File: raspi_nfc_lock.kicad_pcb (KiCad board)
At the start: 2 copper layers, 79 parts, among them J101 Raspberry_Pi_2_3, J102 Screw_Terminal_01x02, J103 Screw_Terminal_01x02, J104 Screw_Terminal_01x02, J105 Screw_Terminal_01x02, J106 Screw_Terminal_01x02, J107 Screw_Terminal_01x02, J108 Screw_Terminal_01x02, J109 Screw_Terminal_01x02, J110 Screw_Terminal_01x02, J111 Screw_Terminal_01x02, J112 Screw_Terminal_01x02, J113 BUZZER, K101 G6E, Q101 MMBT3904, Q102 Si2319CDS, Q103 MMBT3904, U101 74HC14, U102 LM2596S, U103 TXB0104PW

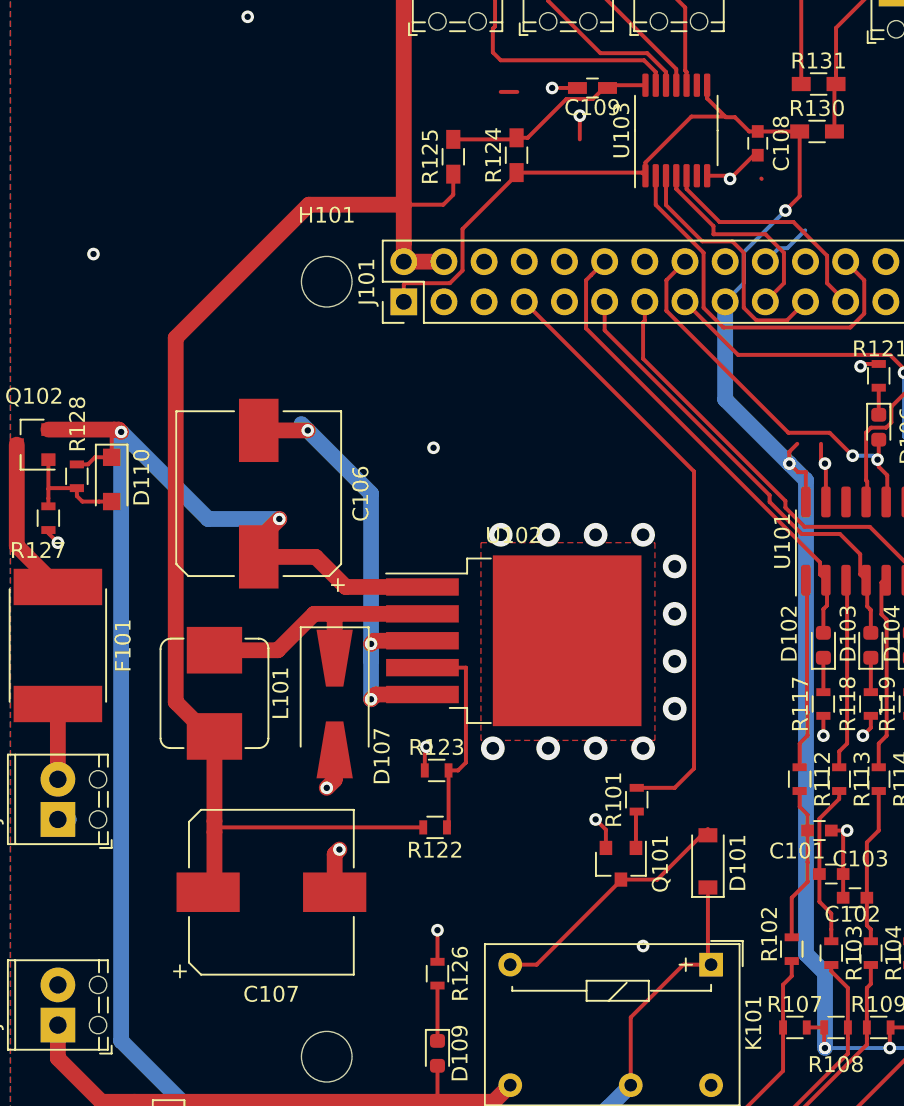
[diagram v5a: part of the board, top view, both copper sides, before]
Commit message: Changed some components to LCSC stock components Added LCSC references for BOM
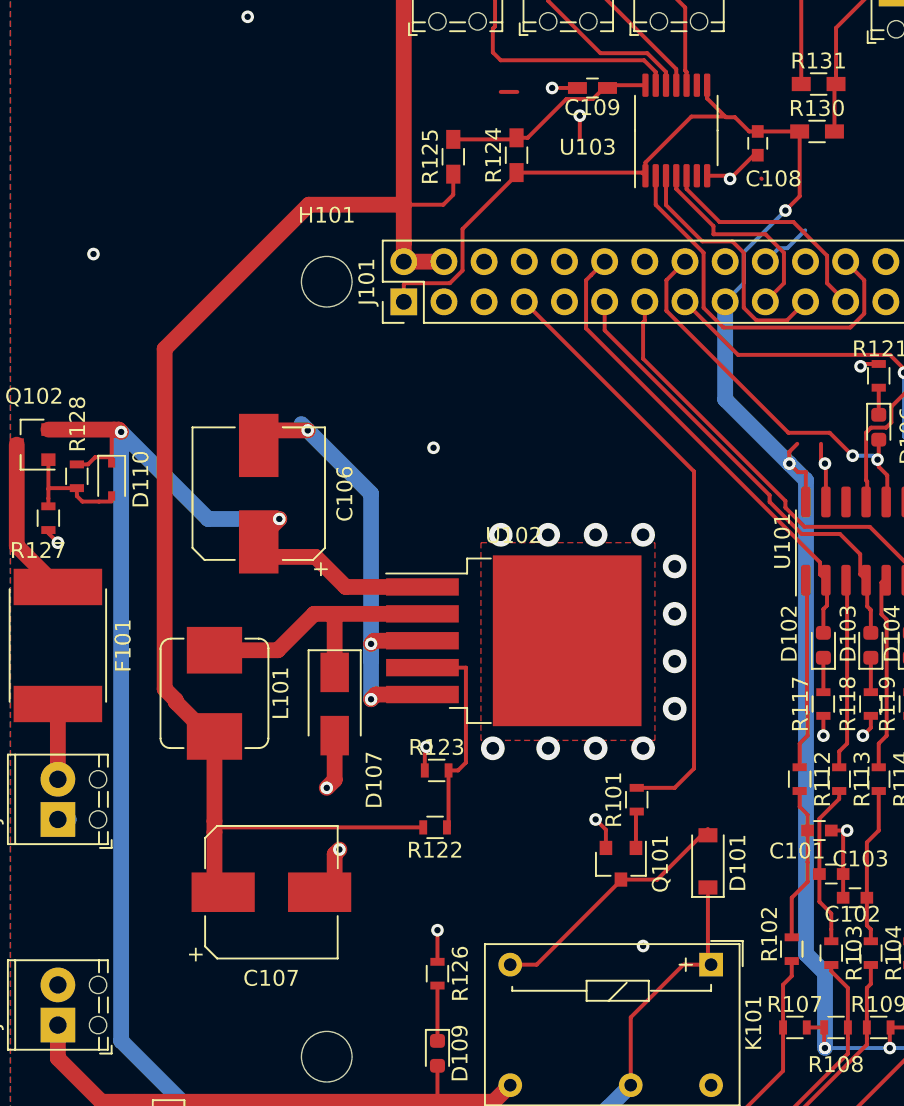
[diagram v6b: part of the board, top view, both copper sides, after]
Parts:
- C106: footprint Capacitors_SMD:CP_Elec_10x10 -> Capacitors_SMD:CP_Elec_8x10
- C107: footprint Capacitors_SMD:CP_Elec_10x10.5 -> Capacitors_SMD:CP_Elec_8x10.5
- D101, D108: value 15V -> SMF15A
- D107: footprint Diodes_SMD:D_SMA-SMB_Universal_Handsoldering -> Diodes_SMD:D_SMA
- D110: footprint Diode_SMD:D_SOD-123F -> Diode_SMD:D_SOD-323
- L101: value SRP7028A-330M -> MWSA0603S-330MT
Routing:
- net +5V: track 144.6 -> 145.2 mm
